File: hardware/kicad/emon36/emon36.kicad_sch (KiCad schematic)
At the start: 76 parts, among them J1 Barrel_Jack, J17 Conn_02x03_Odd_Even, J37 USB_B_Micro, J4 Barrel_Jack, SW2 SW_MEC_5E, SW3 SW_MEC_5E, SW4 SW_MEC_5E, U1 ESP32-C3-WROOM-02-N4, U11 PL133-97QC, U12 PEC12R-4117F-S0012, U3 16.384MHz, U8 TPS5403

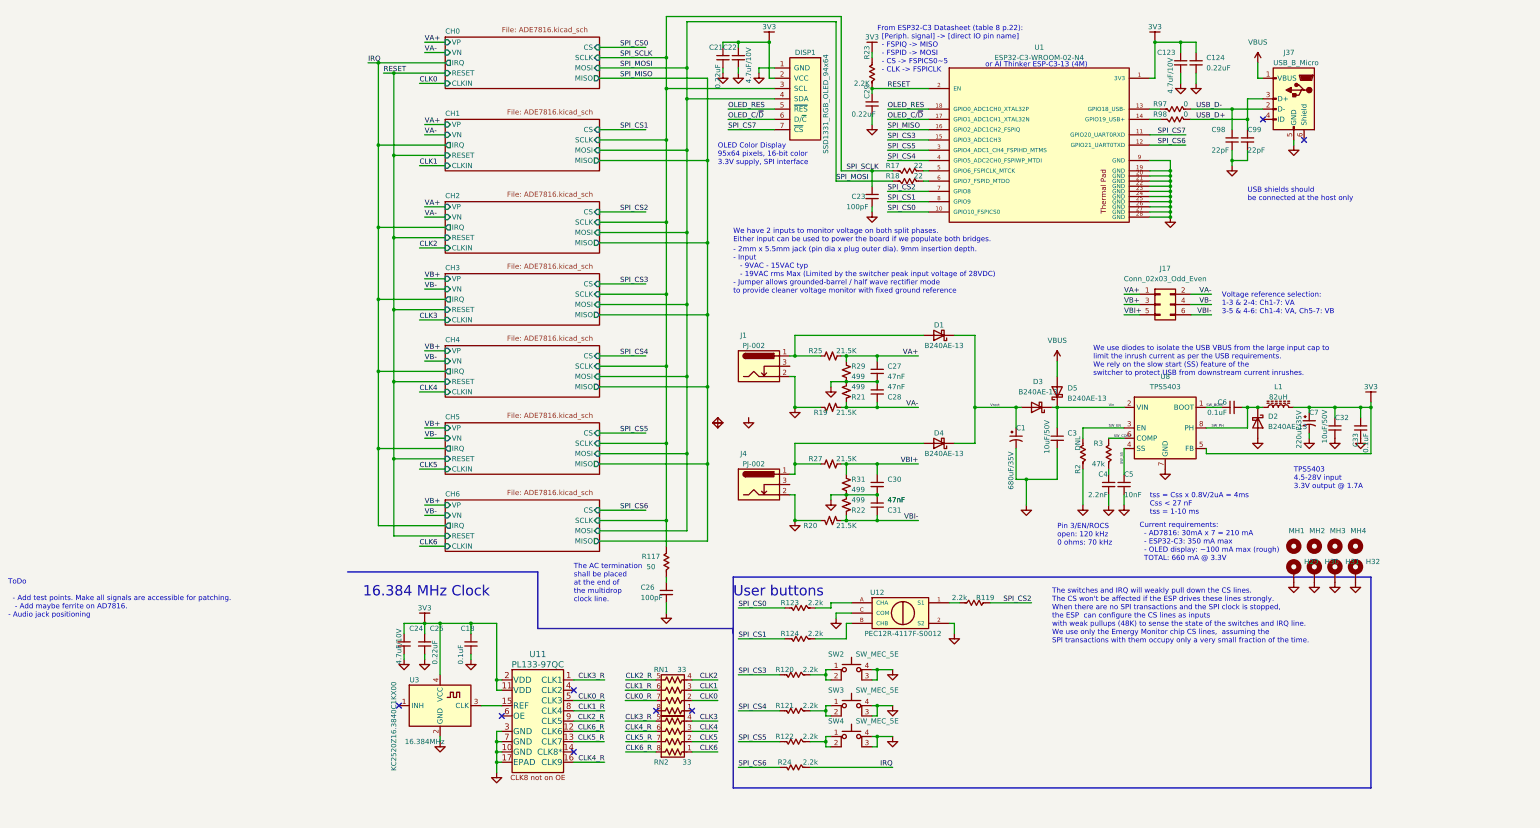
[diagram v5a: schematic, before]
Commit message: Added lots of silkscreen info. Added silk clearance and JLCPCB stackup. Improved Dc-DC with copper pours. Added SPI testpoints.
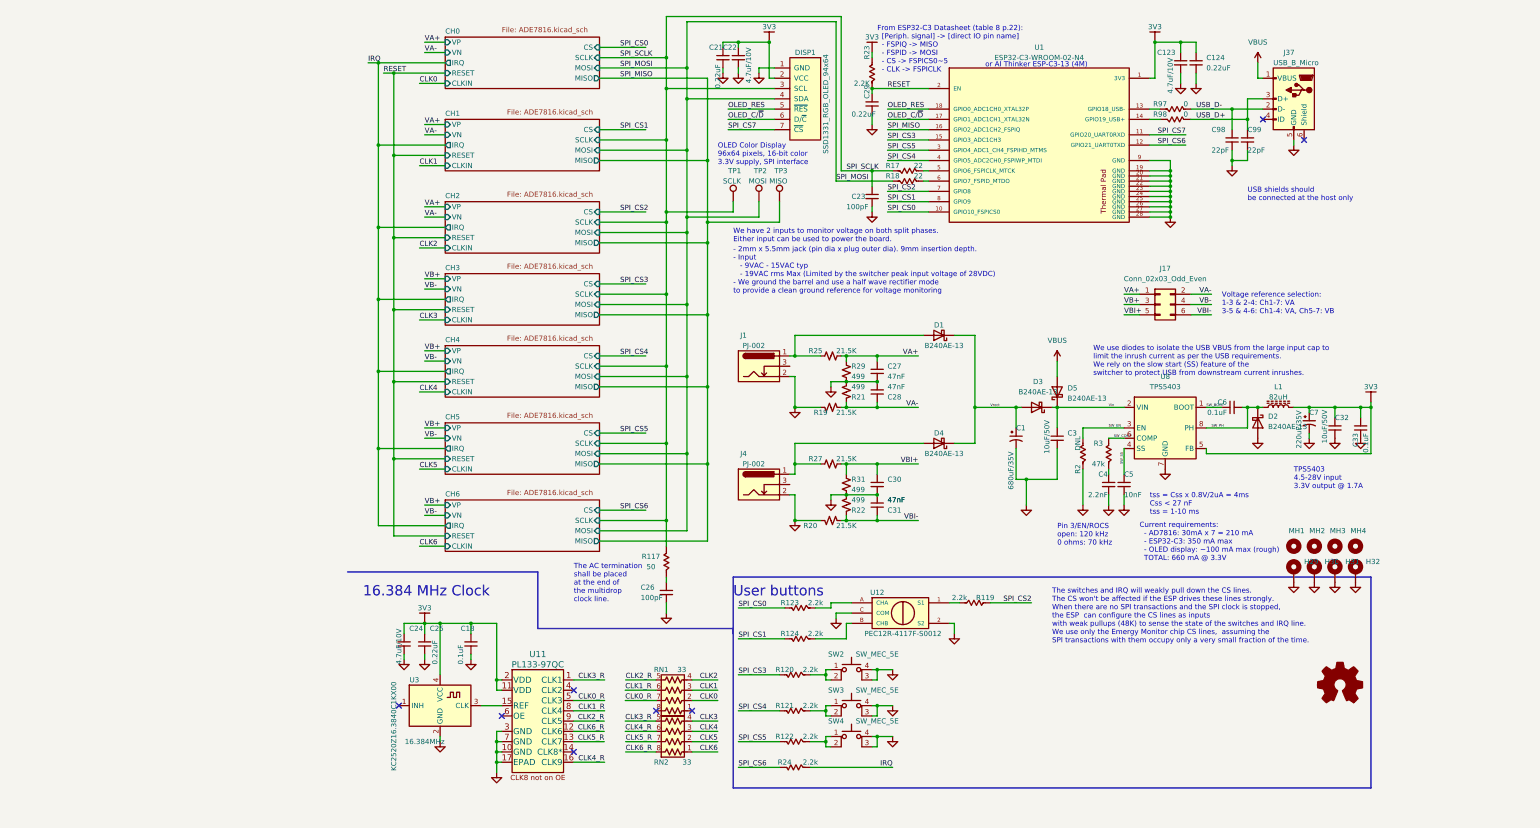
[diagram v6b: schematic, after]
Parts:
- added LOGO1: Logo_Open_Hardware_Small, emon36:OSHW_logo_10mm, symbol Graphic:Logo_Open_Hardware_Small
- added TP1: SCLK, TestPoint:TestPoint_THTPad_D2.0mm_Drill1.0mm, symbol Connector:TestPoint
- added TP2: MOSI, TestPoint:TestPoint_THTPad_D2.0mm_Drill1.0mm, symbol Connector:TestPoint
- added TP3: MISO, TestPoint:TestPoint_THTPad_D2.0mm_Drill1.0mm, symbol Connector:TestPoint
- J37: footprint Connector_USB:USB_Micro-B_Wuerth_629105150521 -> Connector_USB:USB_Micro-B_Amphenol_10118194_Horizontal
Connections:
- net SPI_MISO: now also TP3.1
- net SPI_MOSI: now also TP2.1
- net SPI_SCLK: now also TP1.1
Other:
- note added: "- 2mm x 5.5mm jack (pin dia x plug outer dia). 9mm insertion depth. - Input - 9VAC - 15VAC typ - 19VAC rms Max (Limited by the switcher peak input voltage of 28VDC) - We ground the barrel and use a half wave rectifier mode to provide a clean ground reference for voltage monitoring"
- note added: "OLED Color Display 96x64 pixels, 16-bit color 3.3V supply, SPI interface"
- note added: "We have 2 inputs to monitor voltage on both split phases. Either input can be used to power the board."
- note removed: "- 2mm x 5.5mm jack (pin dia x plug outer dia). 9mm insertion depth. - Input - 9VAC - 15VAC typ - 19VAC rms Max (Limited by the switcher peak input voltage of 28VDC) - Jumper allows grounded-barrel / half wave rectifier mode to provide cleaner voltage monitor with fixed ground reference"
- note removed: "OLED Color Display 95x64 pixels, 16-bit color 3.3V supply, SPI interface"
- note removed: "ToDo - Add test points. Make all signals are accessible for patching. - Add maybe ferrite on AD7816. - Audio jack positioning"
- note removed: "We have 2 inputs to monitor voltage on both split phases. Either input can be used to power the board if we populate both bridges."

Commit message: Schematics: completed/updated some part number fields. Changed 4.7uF to 16V for better effective capacitance. Cleanup top sheet.
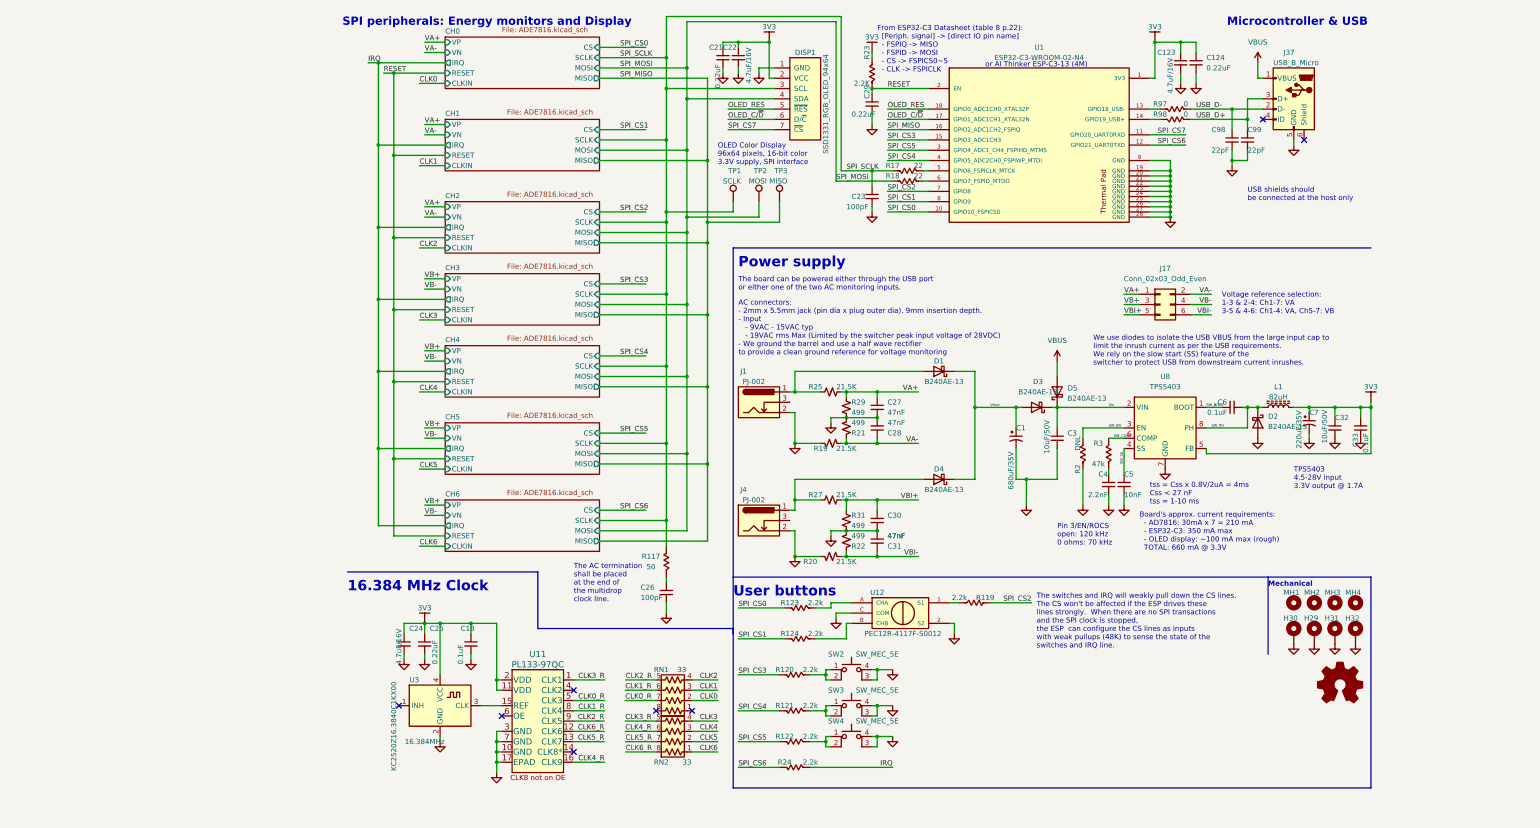
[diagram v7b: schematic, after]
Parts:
- C123, C22, C24: value 4.7uF/10V -> 4.7uF/16V; Desc CAP CER 4.7UF 10V X7S 0603 -> CAP CER 4.7UF 16V X5R 0603; MFR TDK Corporation -> Samsung; MPN C1608X7S1A475K080AC -> CL10A475KO8NNNC
- C7: MFR Robycon -> Rubycon
- J1: footprint Connector_BarrelJack:BarrelJack_Horizontal -> emon36:PJ-002A
- J37: MFR (none) -> Amphenol; MPN (none) -> 10118194-0001LF
- LOGO1, MH1, MH2, MH3, MH4: MFR (none) -> N/A; MPN (none) -> N/A
- RN1, RN2: Desc (none) -> RES ARRAY 4 RES 33 OHM 0804; MFR (none) -> Bourns; MPN (none) -> AT10-330J4LF
- SW2, SW3, SW4: Desc (none) -> SWITCH TACTILE SPST-NO 0.05A 12V
- TP1, TP2, TP3: Desc (none) -> TestPoint; MFR (none) -> N/A; MPN (none) -> N/A
- U1: Desc (none) -> ESP32-C3 MODULE
- U11: Desc (none) -> IC CLK BUFFER 16QFN; MFR (none) -> Microchip Technology; MPN (none) -> PL133-97QC
- U12: Desc (none) -> ROTARY ENCODER MECHANICAL 12PPR; MFR (none) -> Bourns
- U3: Desc (none) -> XTAL OSC XO 16.3840MHZ CMOS SMD
- U8: Desc (none) -> IC REG BUCK 3.3V 1.7A 8SOIC; MFR (none) -> Texas Instruments; MPN (none) -> TPS5403DR
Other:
- note added: "AC connectors: - 2mm x 5.5mm jack (pin dia x plug outer dia). 9mm insertion depth. - Input - 9VAC - 15VAC typ - 19VAC rms Max (Limited by the switcher peak input voltage of 28VDC) - We ground the barrel and use a half wave rectifier to provide a clean ground reference for voltage monitoring"
- note added: "Board's approx. current requirements: - AD7816: 30mA x 7 = 210 mA - ESP32-C3: 350 mA max - OLED display: ~100 mA max (rough) TOTAL: 660 mA @ 3.3V"
- note added: "Mechanical"
- note added: "Microcontroller & USB"
- note added: "Power supply"
- note added: "SPI peripherals: Energy monitors and Display"
- note added: "The board can be powered either through the USB port or either one of the two AC monitoring inputs."
- note added: "The switches and IRQ will weakly pull down the CS lines. The CS won't be affected if the ESP drives these lines strongly. When there are no SPI transactions and the SPI clock is stopped, the ESP can configure the CS lines as inputs with weak pullups (48K) to sense the state of the switches and IRQ line."
- note removed: "- 2mm x 5.5mm jack (pin dia x plug outer dia). 9mm insertion depth. - Input - 9VAC - 15VAC typ - 19VAC rms Max (Limited by the switcher peak input voltage of 28VDC) - We ground the barrel and use a half wave rectifier mode to provide a clean ground reference for voltage monitoring"
- note removed: "Current requirements: - AD7816: 30mA x 7 = 210 mA - ESP32-C3: 350 mA max - OLED display: ~100 mA max (rough) TOTAL: 660 mA @ 3.3V"
- note removed: "The switches and IRQ will weakly pull down the CS lines. The CS won't be affected if the ESP drives these lines strongly. When there are no SPI transactions and the SPI clock is stopped, the ESP can configure the CS lines as inputs with weak pullups (48K) to sense the state of the switches and IRQ line. We use only the Emergy Monitor chip CS lines, assuming the SPI transactions with them occupy o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"
- note removed: "We have 2 inputs to monitor voltage on both split phases. Either input can be used to power the board."
- moved on the sheet: C27, C28, C30, C31, D1, D4, H29, H30, H31, H32, J1, J4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

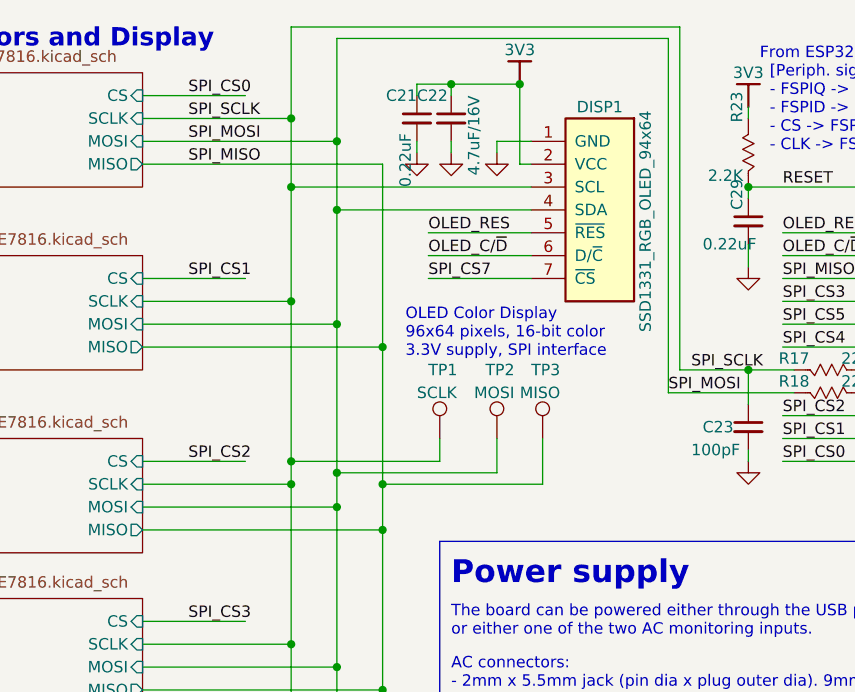
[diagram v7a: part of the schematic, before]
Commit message: Added IRQ diodes - ADE7816 IRQs not open collector. Added pin 1 markers. Increased track widths. Cleanup. Made OLED mounting holes non plated.
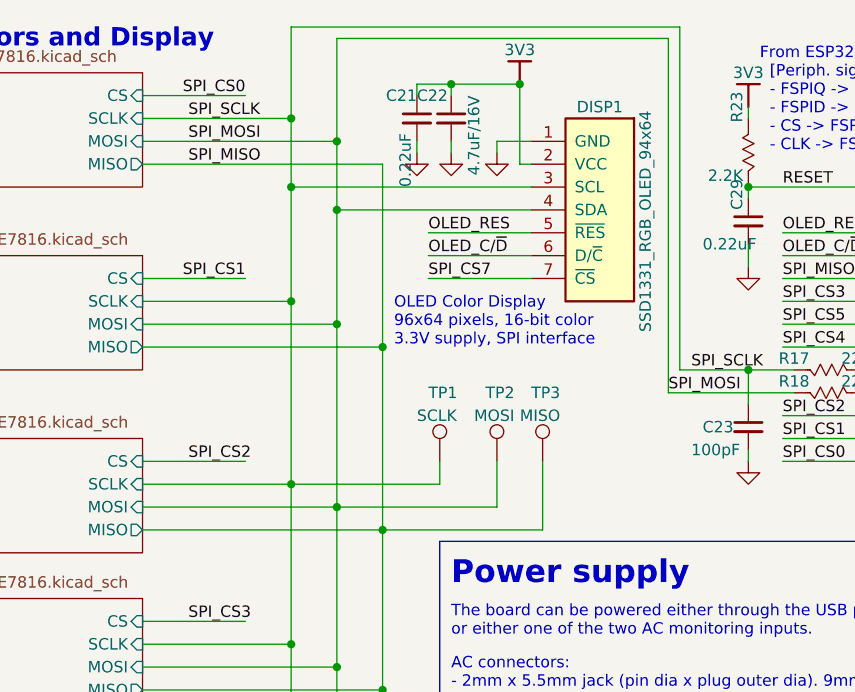
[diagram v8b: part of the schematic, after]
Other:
- moved on the sheet: TP1, TP2, TP3
